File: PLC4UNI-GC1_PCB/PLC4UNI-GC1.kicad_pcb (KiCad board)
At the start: 4 copper layers, 102.4 x 83.1 mm, 179 parts, among them J1 Conn_02x08_Odd_Even, K1 G5V-1, K2 G5V-1, Q1 NCE60P04R, Q2 ZXMS6004FFQTA, Q3 ZXMS6004FFQTA, Q4 ZXMS6004FFQTA, Q5 ZXMS6004FFQTA, SW1 TS-1088-AR02016, U1 ESP32-S3-WROOM-1, U10 ADS1115IDGS, U11 AT3H4B-CUH-S, U12 AT3H4B-CUH-S, U13 LK1802, U14 AT3H4B-CUH-S, U15 MAX31856MUD+, U16 BL0942, U17 B0303S-1WR3_C7465185, U18 ISO7021DR, U2 AT3H4B-CUH-S, U3 AP63203WU, U4 RS485-PROTECT, U5 AT3H4B-CUH-S, U6 AT3H4B-CUH-S, U7 GP8211S-TC50-EW, U8 GP8302-TC50-EW, U9 BTS723GWXUMA1

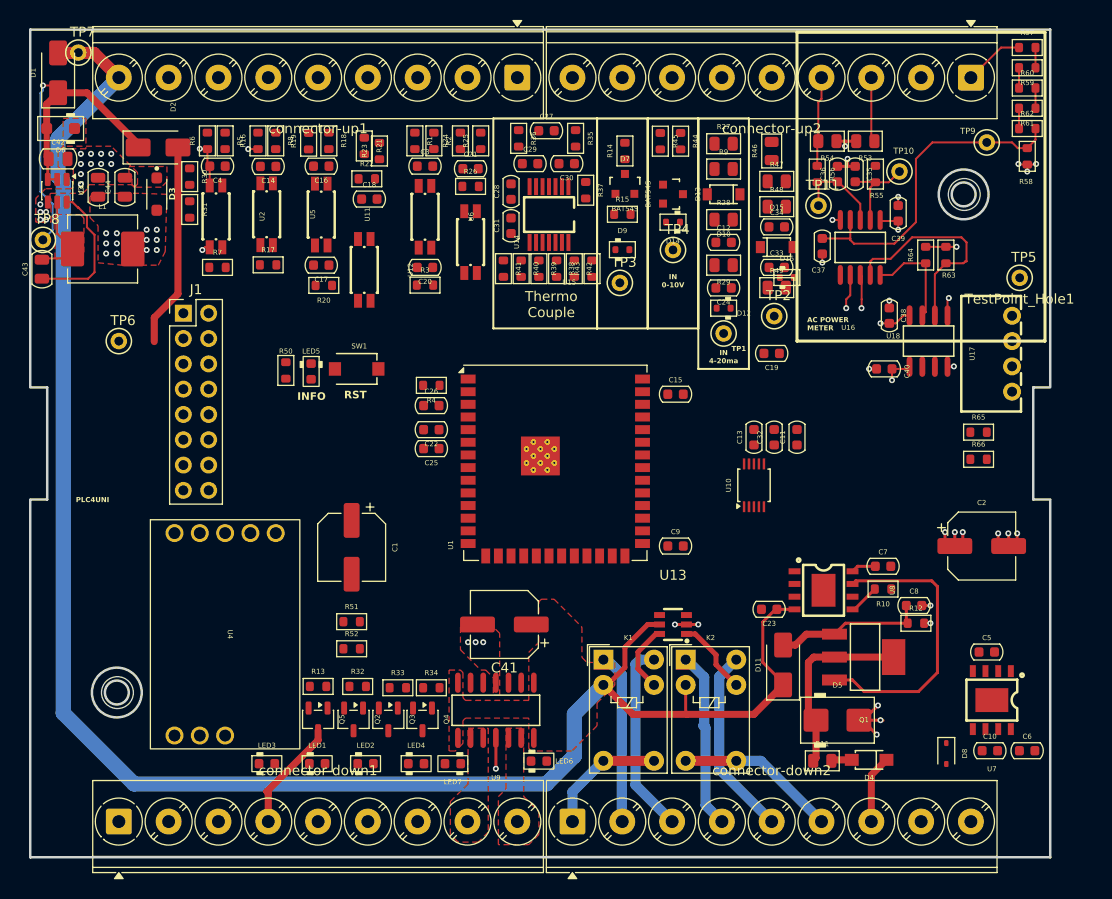
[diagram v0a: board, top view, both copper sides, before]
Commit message: THERMO COUPLE
FINISH DESING
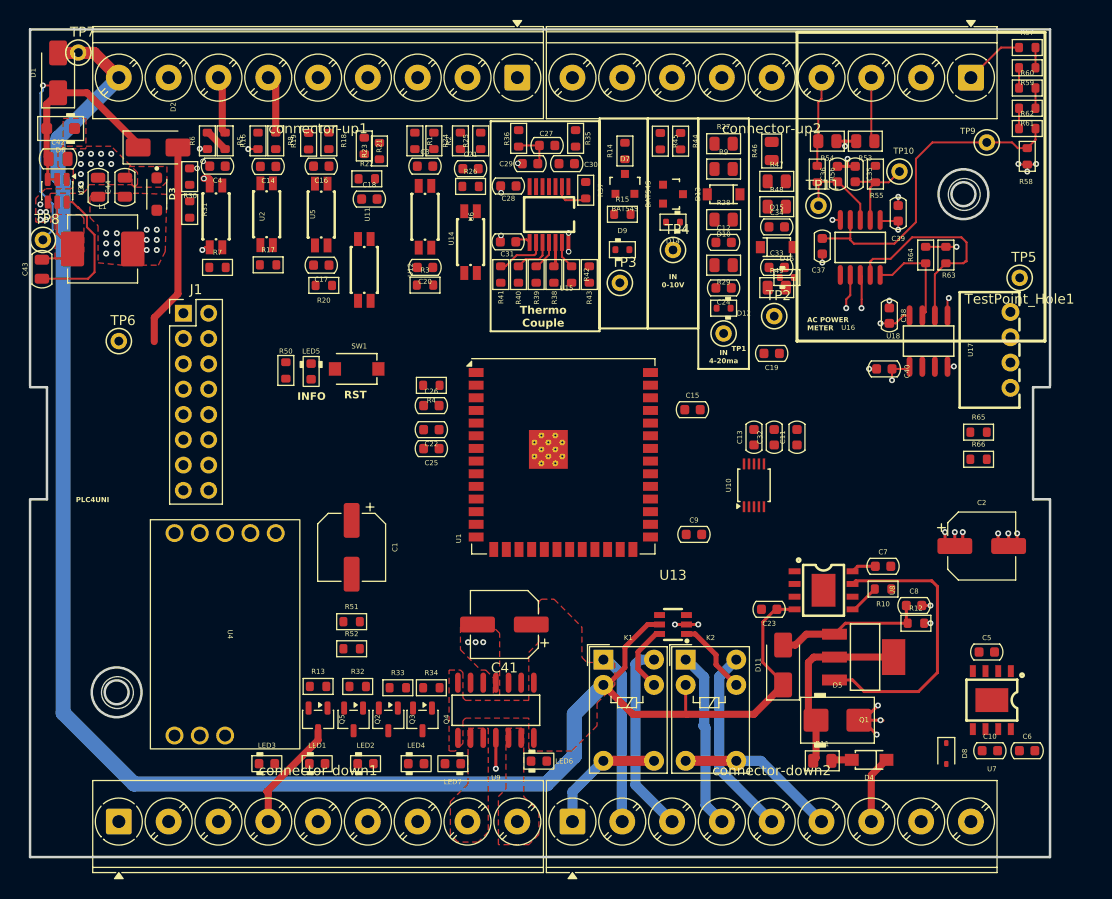
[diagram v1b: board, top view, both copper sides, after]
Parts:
- moved C15 2.30 mm to (153.5, 98.9)
- moved C9 2.19 mm to (153.6, 111.4)
- moved C31 1.64 mm to (135.0, 82.0), turned to 180 degrees
- moved C27 1.48 mm to (138.9, 72.3), turned to 180 degrees
- moved U1 1.03 mm to (140.5, 103.5)
- moved R39 0.65 mm to (137.8, 85.3)
- moved R43 0.65 mm to (143.1, 85.3)
- moved R38 0.65 mm to (139.6, 85.3)
- moved R40 0.65 mm to (136.0, 85.3)
- moved R41 0.65 mm to (134.2, 85.3)
- moved R42 0.65 mm to (141.3, 85.3)
- moved C28 0.62 mm to (135.0, 76.4), turned to 180 degrees
- moved U17 0.42 mm to (185.4, 92.9)
- turned C29 to 180 degrees
- turned C30 to 0 degrees
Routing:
- net /control/CON_IN_NPN2: track 0.00 -> 5.83 mm
- net /control/CON_IN_NPN1: track 0.00 -> 5.80 mm
- net Net-(U15-~{CS}): track 0.00 -> 5.18 mm
- net Net-(U15-SCK): track 0.00 -> 4.17 mm
- net Net-(U15-T+): track 0.00 -> 4.02 mm
- net GND: track 20.5 -> 24.2 mm, vias 31 -> 36
- net Net-(U15-BIAS): track 0.00 -> 3.60 mm
- net Net-(U15-SDO): track 0.00 -> 3.00 mm
- net Net-(U15-~{FAULT}): track 0.00 -> 2.80 mm
- net Net-(U15-SDI): track 0.00 -> 2.46 mm
- net Net-(C4-Pad1): track 0.00 -> 2.46 mm
- net +3.3V: track 10.1 -> 11.7 mm
- net +24V: track 202.6 -> 202.1 mm, vias 2 -> 5
